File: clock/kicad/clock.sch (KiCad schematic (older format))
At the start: 79 parts, among them J1 USB-SS-52100-001, Q1 PN2222A, SW1 HOUR, SW2 MIN, SW3 TIME, U1 74HC4060, U10 74HC390, U11 NE555P, U12 74HC4511, U13 74HC4511, U14 74HC4511, U15 74HC4511, U16 74HC4511, U17 74HC4511, U18 KCSC02-105, U19 KCSC02-105, U2 LD1117V, U20 KCSC02-105, U21 KCSC02-105, U22 KCSC02-105, U23 KCSC02-105, U3 74HC14, U4 74HC157, U5 SN74HC74N, U6 74HC390, U7 74HC08, U8 74HC390, U9 74HC08

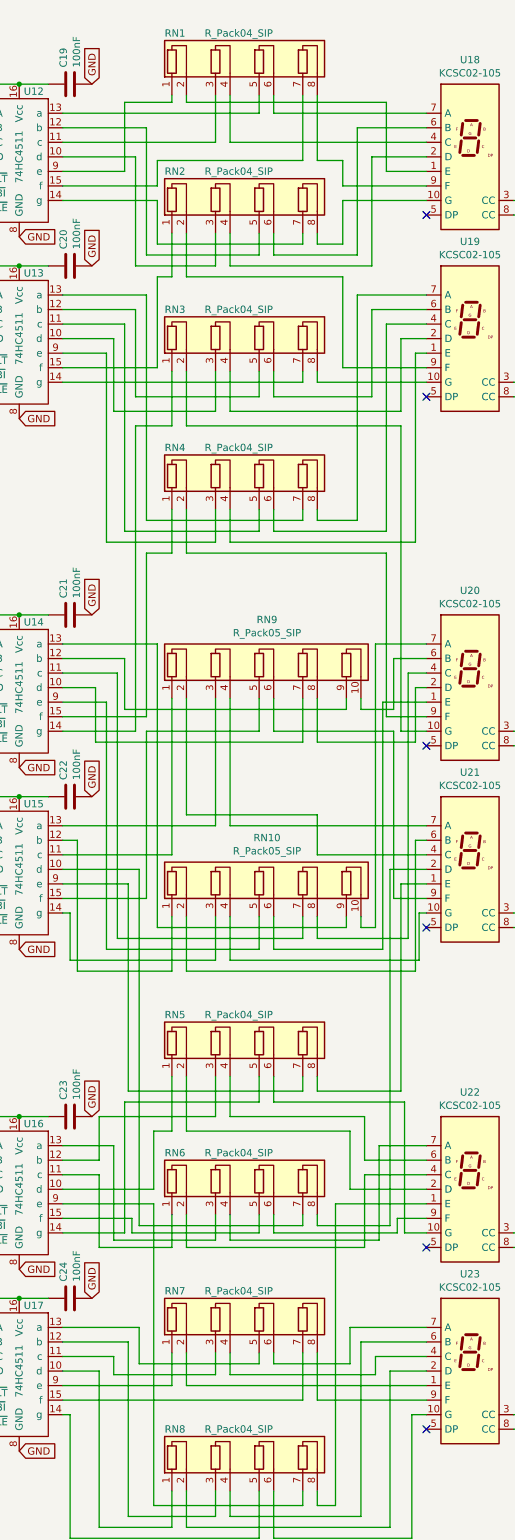
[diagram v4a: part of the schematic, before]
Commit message: Clock: Adjusted LED load resistor values.
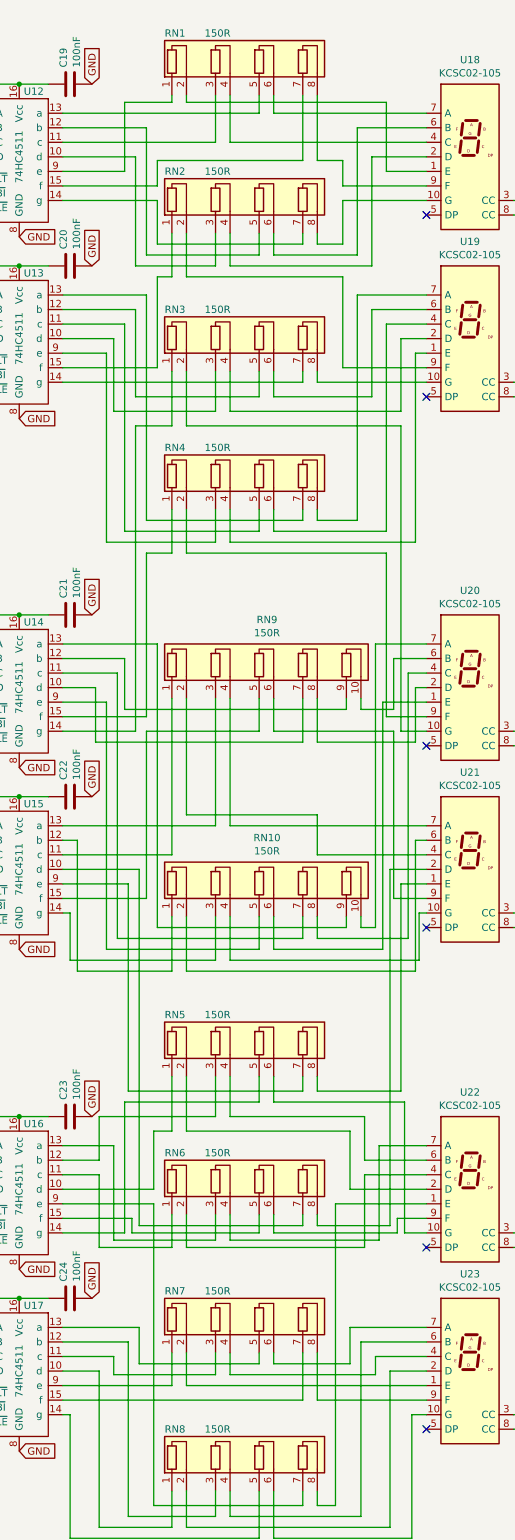
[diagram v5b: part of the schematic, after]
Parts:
- RN1, RN2, RN3, RN4, RN5, RN6, RN7, RN8: value R_Pack04_SIP -> 150R
- RN10, RN9: value R_Pack05_SIP -> 150R
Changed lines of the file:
@@
 P 8750 4975
 F 0 "RN9" H 8804 5317 50  0000 C CNN
-F 1 "R_Pack05_SIP" H 8804 5226 50  0000 C CNN
+F 1 "150R" H 8804 5226 50  0000 C CNN
 F 2 "Resistor_THT:R_Array_SIP10" V 9625 4975 50  0001 C CNN
 F 3 "http://www.vishay.com/docs/31509/csc.pdf" H 8750 4975 50  0001 C CNN
@@
 P 8650 825
 F 0 "RN1" H 8100 1050 50  0000 L CNN
-F 1 "R_Pack04_SIP" H 8375 1050 50  0000 L CNN
+F 1 "150R" H 8375 1050 50  0000 L CNN
 F 2 "Resistor_THT:R_Array_SIP8" V 9325 825 50  0001 C CNN
 F 3 "http://www.vishay.com/docs/31509/csc.pdf" H 8650 825 50  0001 C CNN
@@
 P 8650 1775
 F 0 "RN2" H 8100 2000 50  0000 L CNN
-F 1 "R_Pack04_SIP" H 8375 2000 50  0000 L CNN
+F 1 "150R" H 8375 2000 50  0000 L CNN
 F 2 "Resistor_THT:R_Array_SIP8" V 9325 1775 50  0001 C CNN
 F 3 "http://www.vishay.com/docs/31509/csc.pdf" H 8650 1775 50  0001 C CNN
@@
 P 8650 2725
 F 0 "RN3" H 8100 2950 50  0000 L CNN
-F 1 "R_Pack04_SIP" H 8375 2950 50  0000 L CNN
+F 1 "150R" H 8375 2950 50  0000 L CNN
 F 2 "Resistor_THT:R_Array_SIP8" V 9325 2725 50  0001 C CNN
 F 3 "http://www.vishay.com/docs/31509/csc.pdf" H 8650 2725 50  0001 C CNN
@@
 P 8650 3675
 F 0 "RN4" H 8100 3900 50  0000 L CNN
-F 1 "R_Pack04_SIP" H 8375 3900 50  0000 L CNN
+F 1 "150R" H 8375 3900 50  0000 L CNN
 F 2 "Resistor_THT:R_Array_SIP8" V 9325 3675 50  0001 C CNN
 F 3 "http://www.vishay.com/docs/31509/csc.pdf" H 8650 3675 50  0001 C CNN
@@
 P 8750 6475
 F 0 "RN10" H 8804 6817 50  0000 C CNN
-F 1 "R_Pack05_SIP" H 8804 6726 50  0000 C CNN
+F 1 "150R" H 8804 6726 50  0000 C CNN
 F 2 "Resistor_THT:R_Array_SIP10" V 9625 6475 50  0001 C CNN
 F 3 "http://www.vishay.com/docs/31509/csc.pdf" H 8750 6475 50  0001 C CNN
@@
 P 8650 7575
 F 0 "RN5" H 8100 7800 50  0000 L CNN
-F 1 "R_Pack04_SIP" H 8375 7800 50  0000 L CNN
+F 1 "150R" H 8375 7800 50  0000 L CNN
 F 2 "Resistor_THT:R_Array_SIP8" V 9325 7575 50  0001 C CNN
 F 3 "http://www.vishay.com/docs/31509/csc.pdf" H 8650 7575 50  0001 C CNN
@@
 P 8650 8525
 F 0 "RN6" H 8100 8750 50  0000 L CNN
-F 1 "R_Pack04_SIP" H 8375 8750 50  0000 L CNN
+F 1 "150R" H 8375 8750 50  0000 L CNN
 F 2 "Resistor_THT:R_Array_SIP8" V 9325 8525 50  0001 C CNN
 F 3 "http://www.vishay.com/docs/31509/csc.pdf" H 8650 8525 50  0001 C CNN
@@
 P 8650 9475
 F 0 "RN7" H 8100 9700 50  0000 L CNN
-F 1 "R_Pack04_SIP" H 8375 9700 50  0000 L CNN
+F 1 "150R" H 8375 9700 50  0000 L CNN
 F 2 "Resistor_THT:R_Array_SIP8" V 9325 9475 50  0001 C CNN
 F 3 "http://www.vishay.com/docs/31509/csc.pdf" H 8650 9475 50  0001 C CNN
@@
 P 8650 10425
 F 0 "RN8" H 8100 10650 50  0000 L CNN
-F 1 "R_Pack04_SIP" H 8375 10650 50  0000 L CNN
+F 1 "150R" H 8375 10650 50  0000 L CNN
 F 2 "Resistor_THT:R_Array_SIP8" V 9325 10425 50  0001 C CNN
 F 3 "http://www.vishay.com/docs/31509/csc.pdf" H 8650 10425 50  0001 C CNN

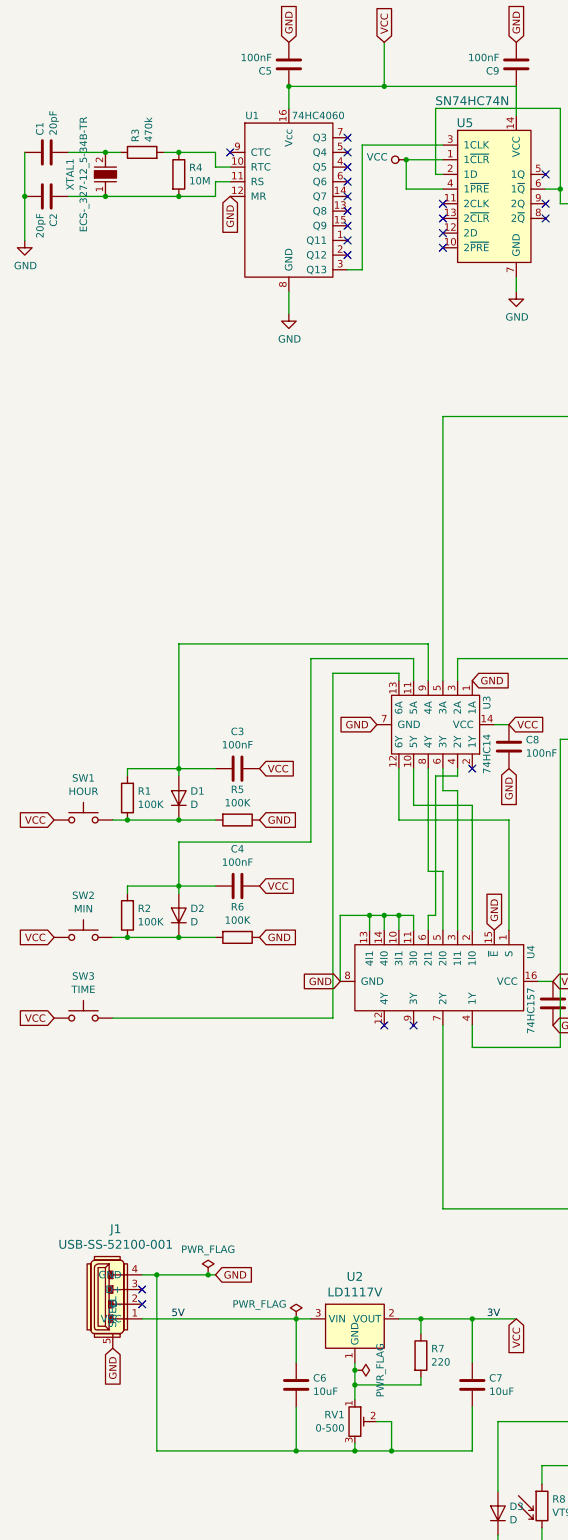
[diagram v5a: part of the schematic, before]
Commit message: Clock: Added Bill Of Materials.
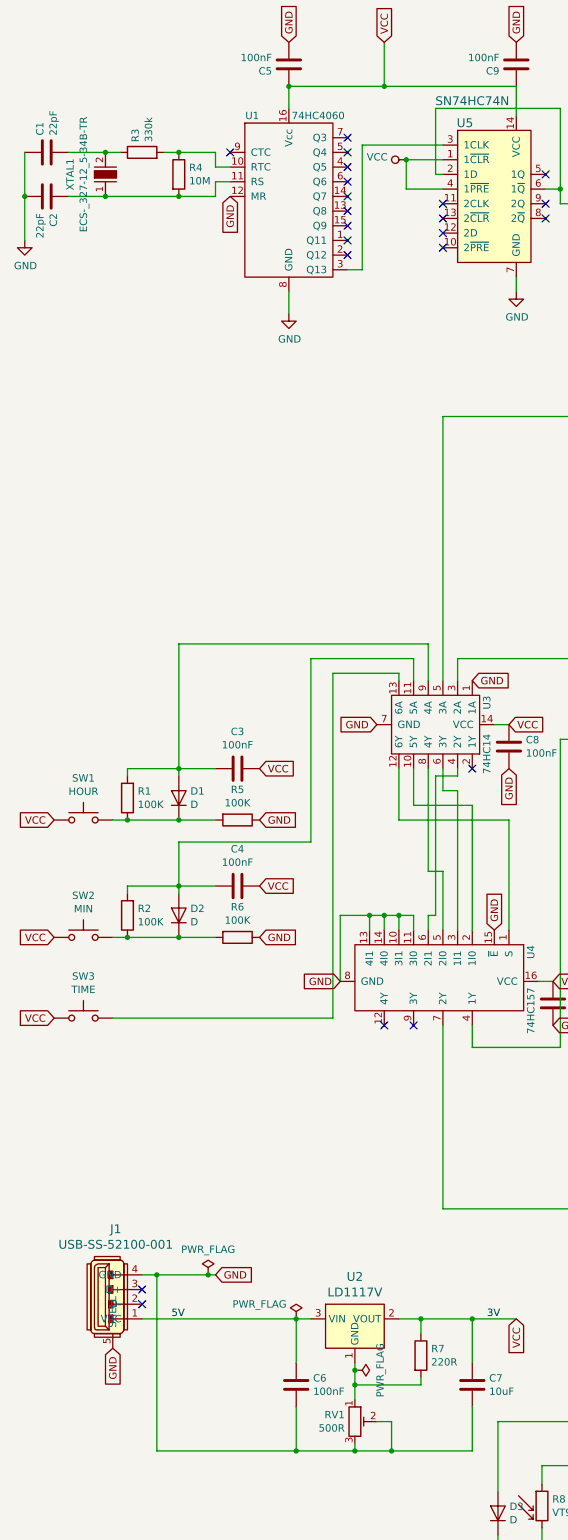
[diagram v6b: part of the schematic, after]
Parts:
- C1, C2: value 20pF -> 22pF
- C6: value 10uF -> 100nF
- R3: value 470k -> 330k
- R7: value 220 -> 220R
- RV1: value 0-500 -> 500R
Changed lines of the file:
@@
 P 1550 1500
 F 0 "R3" H 1620 1546 50  0000 L CNN
-F 1 "470k" H 1620 1455 50  0000 L CNN
+F 1 "330k" H 1620 1455 50  0000 L CNN
 F 2 "Resistor_THT:R_Axial_DIN0207_L6.3mm_D2.5mm_P7.62mm_Horizontal" V 1480 1500 50  0001 C CNN
 F 3 "~" H 1550 1500 50  0001 C CNN
@@
 P 900 1800
 F 0 "C2" H 1015 1846 50  0000 L CNN
-F 1 "20pF" H 1015 1755 50  0000 L CNN
+F 1 "22pF" H 1015 1755 50  0000 L CNN
 F 2 "Capacitor_THT:C_Disc_D5.0mm_W2.5mm_P2.50mm" H 938 1650 50  0001 C CNN
 F 3 "~" H 900 1800 50  0001 C CNN
@@
 P 900 1500
 F 0 "C1" H 1015 1546 50  0000 L CNN
-F 1 "20pF" H 1015 1455 50  0000 L CNN
+F 1 "22pF" H 1015 1455 50  0000 L CNN
 F 2 "Capacitor_THT:C_Disc_D5.0mm_W2.5mm_P2.50mm" H 938 1350 50  0001 C CNN
 F 3 "~" H 900 1500 50  0001 C CNN
@@
 P 2600 9900
 F 0 "C6" H 2715 9946 50  0000 L CNN
-F 1 "10uF" H 2715 9855 50  0000 L CNN
+F 1 "100nF" H 2715 9855 50  0000 L CNN
 F 2 "Capacitor_THT:C_Disc_D5.0mm_W2.5mm_P2.50mm" H 2638 9750 50  0001 C CNN
 F 3 "~" H 2600 9900 50  0001 C CNN
@@
 P 3450 9700
 F 0 "R7" H 3520 9746 50  0000 L CNN
-F 1 "220" H 3520 9655 50  0000 L CNN
+F 1 "220R" H 3520 9655 50  0000 L CNN
 F 2 "Resistor_THT:R_Axial_DIN0207_L6.3mm_D2.5mm_P7.62mm_Horizontal" V 3380 9700 50  0001 C CNN
 F 3 "~" H 3450 9700 50  0001 C CNN
@@
 U 1 1 610D8243
 P 3000 10150
-F 0 "RV1" H 2930 10196 50  0000 R CNN
-F 1 "0-500" H 2930 10105 50  0000 R CNN
+F 0 "RV1" H 2931 10196 50  0000 R CNN
+F 1 "500R" H 2931 10105 50  0000 R CNN
 F 2 "Potentiometer_THT:Potentiometer_Bourns_3339P_Vertical_HandSoldering" H 3000 10150 50  0001 C CNN
 F 3 "~" H 3000 10150 50  0001 C CNN

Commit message: Clock: Added missing pulldown resistor to Time button.
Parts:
- added R7: 100K, Resistor_THT:R_Axial_DIN0207_L6.3mm_D2.5mm_P7.62mm_Horizontal, symbol Device:R
- renumbered R9 to R10, R10 to R11, R11 to R12, R7 to R8, R8 to R9
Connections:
- net GND: now also R7.1
- net at SW3.2, U3.13 (6A): now also R7.2
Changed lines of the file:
@@
 Wire Wire Line
 	1800 6200 1800 6500
-Wire Wire Line
-	1350 7400 2850 7400
 Text GLabel 3150 5400 0    50   Input ~ 0
 GND
@@
 VCC
 Wire Wire Line
-	2850 7400 2850 5050
-Wire Wire Line
-	2850 5050 3300 5050
+	2800 5050 3300 5050
 Wire Wire Line
 	3300 5050 3300 5100
@@
 $EndComp
 $Comp
-L Device:R R9
+L Device:R R10
 U 1 1 5DB7BBEA
 P 4675 10725
-F 0 "R9" H 4605 10679 50  0000 R CNN
+F 0 "R10" H 4605 10679 50  0000 R CNN
 F 1 "1M" H 4605 10770 50  0000 R CNN
 F 2 "Resistor_THT:R_Axial_DIN0207_L6.3mm_D2.5mm_P7.62mm_Horizontal" V 4605 10725 50  0001 C CNN
@@
 	6400 10150 5350 10150
 $Comp
-L Sensor_Optical:VT93xx R8
+L Sensor_Optical:VT93xx R9
 U 1 1 5DC80BDF
 P 4275 10725
-F 0 "R8" H 4345 10771 50  0000 L CNN
+F 0 "R9" H 4345 10771 50  0000 L CNN
 F 1 "VT93xx" H 4345 10680 50  0000 L CNN
 F 2 "OptoDevice:R_LDR_4.9x4.2mm_P2.54mm_Vertical" V 4450 10725 50  0001 C CNN
@@
 	6250 11350 6550 11350
 $Comp
-L Device:R R11
+L Device:R R12
 U 1 1 5DEB054B
 P 6700 11350
-F 0 "R11" H 6630 11304 50  0000 R CNN
+F 0 "R12" H 6630 11304 50  0000 R CNN
 F 1 "5.1K" H 6630 11395 50  0000 R CNN
 F 2 "Resistor_THT:R_Axial_DIN0207_L6.3mm_D2.5mm_P7.62mm_Horizontal" V 6630 11350 50  0001 C CNN
@@
 	7450 11550 7450 11675
 $Comp
-L Device:R R10
+L Device:R R11
 U 1 1 5E34B6A6
 P 5350 10550
-F 0 "R10" H 5280 10504 50  0000 R CNN
+F 0 "R11" H 5280 10504 50  0000 R CNN
 F 1 "10K" H 5280 10595 50  0000 R CNN
 F 2 "Resistor_THT:R_Axial_DIN0207_L6.3mm_D2.5mm_P7.62mm_Horizontal" V 5280 10550 50  0001 C CNN
@@
 	1550 9150 1650 9150
 $Comp
-L Device:R R7
+L Device:R R8
 U 1 1 5DA44C3B
 P 3450 9700
-F 0 "R7" H 3520 9746 50  0000 L CNN
+F 0 "R8" H 3520 9746 50  0000 L CNN
 F 1 "220R" H 3520 9655 50  0000 L CNN
 F 2 "Resistor_THT:R_Axial_DIN0207_L6.3mm_D2.5mm_P7.62mm_Horizontal" V 3380 9700 50  0001 C CNN
@@
 Wire Wire Line
 	8250 9900 9900 9900
+$Comp
+L Device:R R7
+U 1 1 644D937E
+P 2200 7400
+F 0 "R7" V 1993 7400 50  0000 C CNN
+F 1 "100K" V 2084 7400 50  0000 C CNN
+F 2 "Resistor_THT:R_Axial_DIN0207_L6.3mm_D2.5mm_P7.62mm_Horizontal" V 2130 7400 50  0001 C CNN
+F 3 "~" H 2200 7400 50  0001 C CNN
+	1    2200 7400
+	0    1    1    0
+$EndComp
+Text GLabel 2350 7400 2    50   Input ~ 0
+GND
+Wire Wire Line
+	1350 7400 1800 7400
+Wire Wire Line
+	2800 7025 1800 7025
+Wire Wire Line
+	1800 7025 1800 7400
+Wire Wire Line
+	2800 5050 2800 7025
+Connection ~ 1800 7400
+Wire Wire Line
+	1800 7400 2050 7400
 $EndSCHEMATC

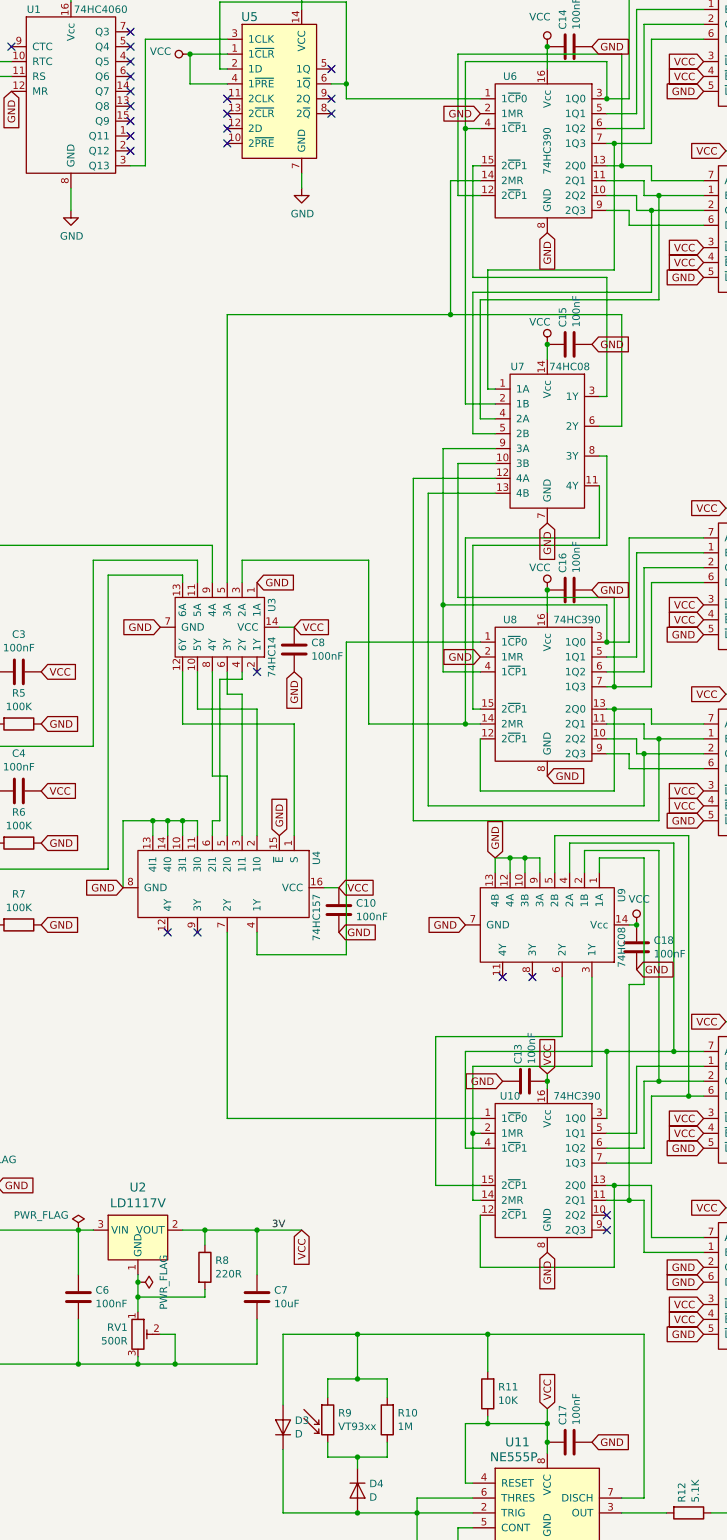
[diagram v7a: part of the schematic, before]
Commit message: Clock: Time Switch Resets Seconds.
Added a two-diode OR gate to use the Time switch as a secondary input
for the seconds counter's reset lines.
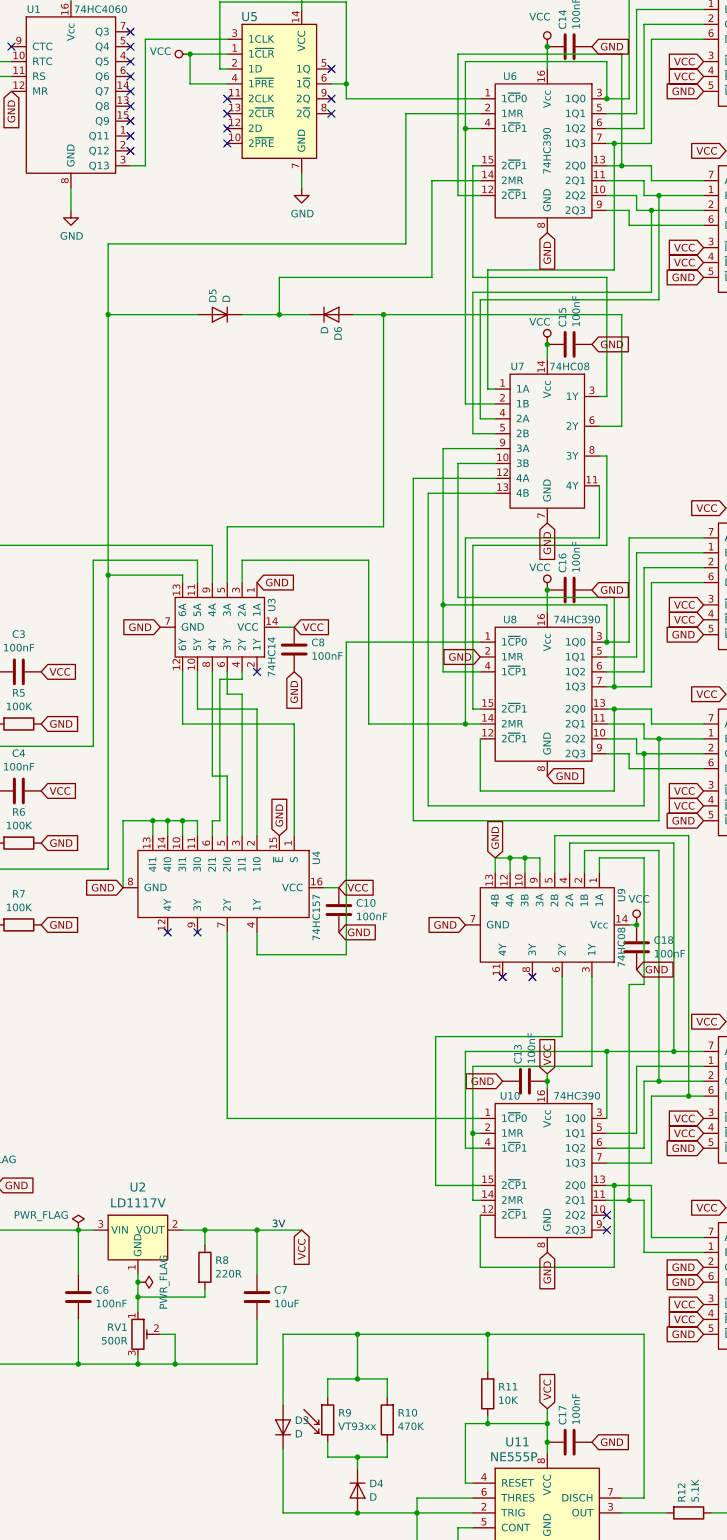
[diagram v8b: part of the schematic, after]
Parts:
- added D5, D6: D, digikey-footprints:Diode_DO-35_P10mm, symbol Device:D
- R10: value 1M -> 470K
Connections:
- net GND: no longer U6.2 (1MR)
- net at U3.5 (3A), U7.6 (2Y): now also D6.2 (A); no longer U6.14 (2MR)
- net at R7.2, SW3.2, U3.13 (6A): now also U6.2 (1MR), D5.2 (A)
- new net: D5.1 (K), D6.1 (K), U6.14 (2MR)
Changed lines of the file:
@@
 	6250 2300 6450 2300
-Wire Wire Line
-	5300 2400 5100 2400
 Wire Wire Line
 	5150 2500 5300 2500
@@
 Wire Wire Line
 	6500 3200 6500 2500
-Wire Wire Line
-	5100 2400 5100 3300
-Wire Wire Line
-	5100 3300 6250 3300
 Text GLabel 6800 1700 0    50   Input ~ 0
 VCC
@@
 	4850 4400 5400 4400
 Text GLabel 5750 2750 3    50   Input ~ 0
-GND
-Text GLabel 5300 1950 0    50   Input ~ 0
 GND
 $Comp
@@
 Wire Wire Line
 	3400 5700 3400 5950
-Wire Wire Line
-	5100 3300 3600 3300
-Wire Wire Line
-	3600 3300 3600 5100
-Connection ~ 5100 3300
 Text GLabel 3800 5100 2    50   Input ~ 0
 GND
@@
 P 4675 10725
 F 0 "R10" H 4605 10679 50  0000 R CNN
-F 1 "1M" H 4605 10770 50  0000 R CNN
+F 1 "470K" H 4605 10770 50  0000 R CNN
 F 2 "Resistor_THT:R_Axial_DIN0207_L6.3mm_D2.5mm_P7.62mm_Horizontal" V 4605 10725 50  0001 C CNN
 F 3 "~" H 4675 10725 50  0001 C CNN
@@
 Wire Wire Line
 	1800 7400 2050 7400
+$Comp
+L Device:D D6
+U 1 1 64871AD3
+P 4300 3300
+F 0 "D6" V 4346 3221 50  0000 R CNN
+F 1 "D" V 4255 3221 50  0000 R CNN
+F 2 "digikey-footprints:Diode_DO-35_P10mm" H 4300 3300 50  0001 C CNN
+F 3 "~" H 4300 3300 50  0001 C CNN
+	1    4300 3300
+	1    0    0    -1
+$EndComp
+$Comp
+L Device:D D5
+U 1 1 64873A41
+P 3550 3300
+F 0 "D5" V 3596 3221 50  0000 R CNN
+F 1 "D" V 3505 3221 50  0000 R CNN
+F 2 "digikey-footprints:Diode_DO-35_P10mm" H 3550 3300 50  0001 C CNN
+F 3 "~" H 3550 3300 50  0001 C CNN
+	1    3550 3300
+	-1   0    0    1
+$EndComp
+Connection ~ 2800 5050
+Wire Wire Line
+	3950 3050 4975 3050
+Wire Wire Line
+	4975 3050 4975 2400
+Wire Wire Line
+	4975 2400 5300 2400
+Wire Wire Line
+	2800 2825 4800 2825
+Wire Wire Line
+	4800 2825 4800 1950
+Wire Wire Line
+	4800 1950 5300 1950
+Wire Wire Line
+	3600 5100 3600 4725
+Wire Wire Line
+	3600 4725 4650 4725
+Wire Wire Line
+	4650 4725 4650 3300
+Wire Wire Line
+	4650 3300 6250 3300
+Wire Wire Line
+	4450 3300 4650 3300
+Connection ~ 4650 3300
+Wire Wire Line
+	3700 3300 3950 3300
+Wire Wire Line
+	3950 3050 3950 3300
+Connection ~ 3950 3300
+Wire Wire Line
+	3950 3300 4150 3300
+Wire Wire Line
+	2800 2825 2800 3300
+Wire Wire Line
+	3400 3300 2800 3300
+Connection ~ 2800 3300
+Wire Wire Line
+	2800 3300 2800 5050
 $EndSCHEMATC
